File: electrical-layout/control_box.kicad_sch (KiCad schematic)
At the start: 5 parts, among them U14 PCB03, U18 NO Switch

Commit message: layout-2025: update many parts of the layout
What a goooood commit message!

... sorry
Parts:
- removed F6: 15A, symbol Device:Fuse
- removed U18: NO Switch, symbol Exocet:VC_Switch_NO
- added J6: Telemetry Battery Charge Connector, symbol Connector_Generic:Conn_01x02
- added J7: Tracking Device Connector, symbol Connector_Generic:Conn_01x02
- added K6: Telemetry Battery Relay, symbol Relay:Relay_SPST-NO
- added U12, U13, U9: Valve Actuator, symbol Exocet:Hanbay_Valve_Actuator
- added U24: Connection PCB, symbol Exocet:Connection_PCB
- added U25, U26: Temperature Sensor, Package_TO_SOT_THT:TO-92_Inline, symbol Sensor_Temperature:DS18B20
- added U27: H2 Control PCB, symbol Exocet:H2_Control_Pcb
- added U28, U29: Manometer, symbol Exocet:Swagelok_Manometer
- added U4: (no value), symbol Exocet:Power_Control_Pcb
- U14: value PCB03 -> Telemetry Battery PCB; DIST (none) -> JLCPCB; MFR (none) -> Exocet; MPN (none) -> PCB03
- U15: value ~ -> Cooling System; Manufacturer TBD -> (none); Part TBD -> (none)
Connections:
- net +48V: now also U4. (GATE); no longer U15. (GND)
- net GND: now also U4. (GATE); no longer U15. (GND)
- net at BT3.1 (+): now also J6.2 (Pin_2), K6.14
- net Frame: now reaches BT3.2 (-), U14. (GND)
- net Frame: now also J6.1 (Pin_1), J7.2 (Pin_2), K6.A2
- new net: U14. (GND), U25.1 (GND)
- new net: U14. (GND), U25.2 (DQ)
- new net: U14. (GND), U25.3 (V_{DD})
- new net: J7.1 (Pin_1), K6.13, U14. (GND)
- new net: U15. (GND), U26.1 (GND)
- new net: U15. (GND), U26.2 (DQ)
- new net: U15. (GND), U26.3 (V_{DD})
- new net BOP+: U15. (GND)
- new net BOP_CTRL_G: U4. (GATE)
- new net BOP_CTRL_S: U4. (GATE)
- new net BRAKE_CTRL_G: U4. (GATE)
- new net BRAKE_CTRL_S: U4. (GATE)
- new net CHARGE_UART: U4. (GATE)
- new net FC_CTRL_G: U4. (GATE)
- new net FC_CTRL_S: U4. (GATE)
- new net FC_UART: U4. (GATE)
- new net HV_BUS-: U15. (GND)
- new net MOTOR_CTRL_G: U4. (GATE)
- new net MOTOR_CTRL_S: U4. (GATE)
- no-connect marks 0 -> 24

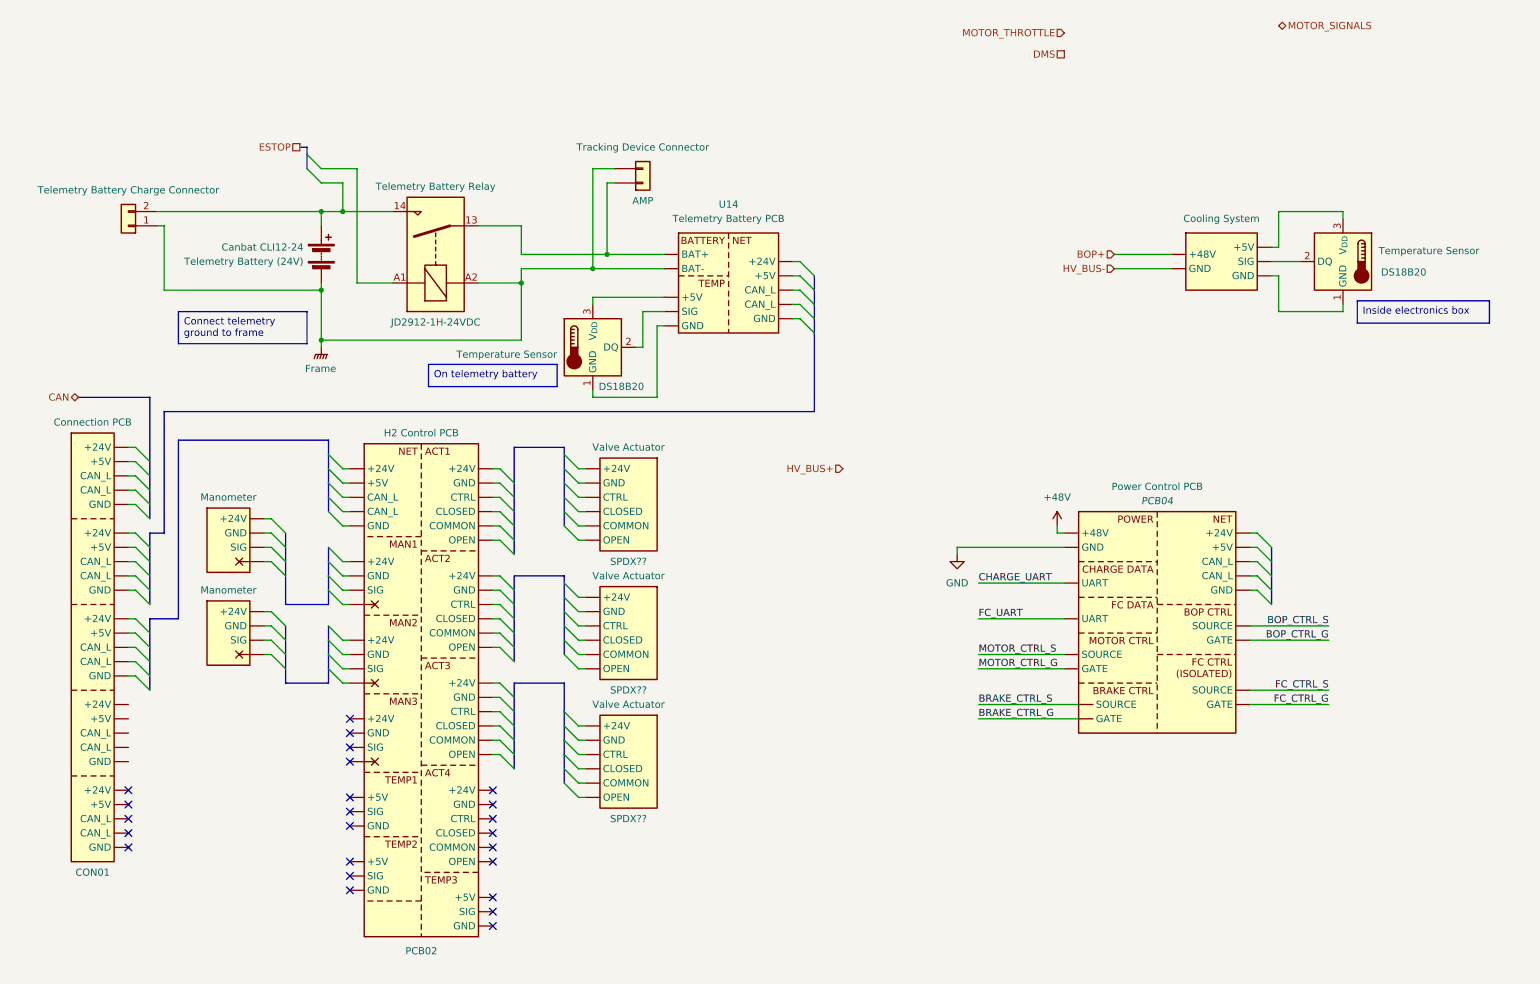
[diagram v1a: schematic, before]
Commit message: layout-2025: add power breadboard and connections
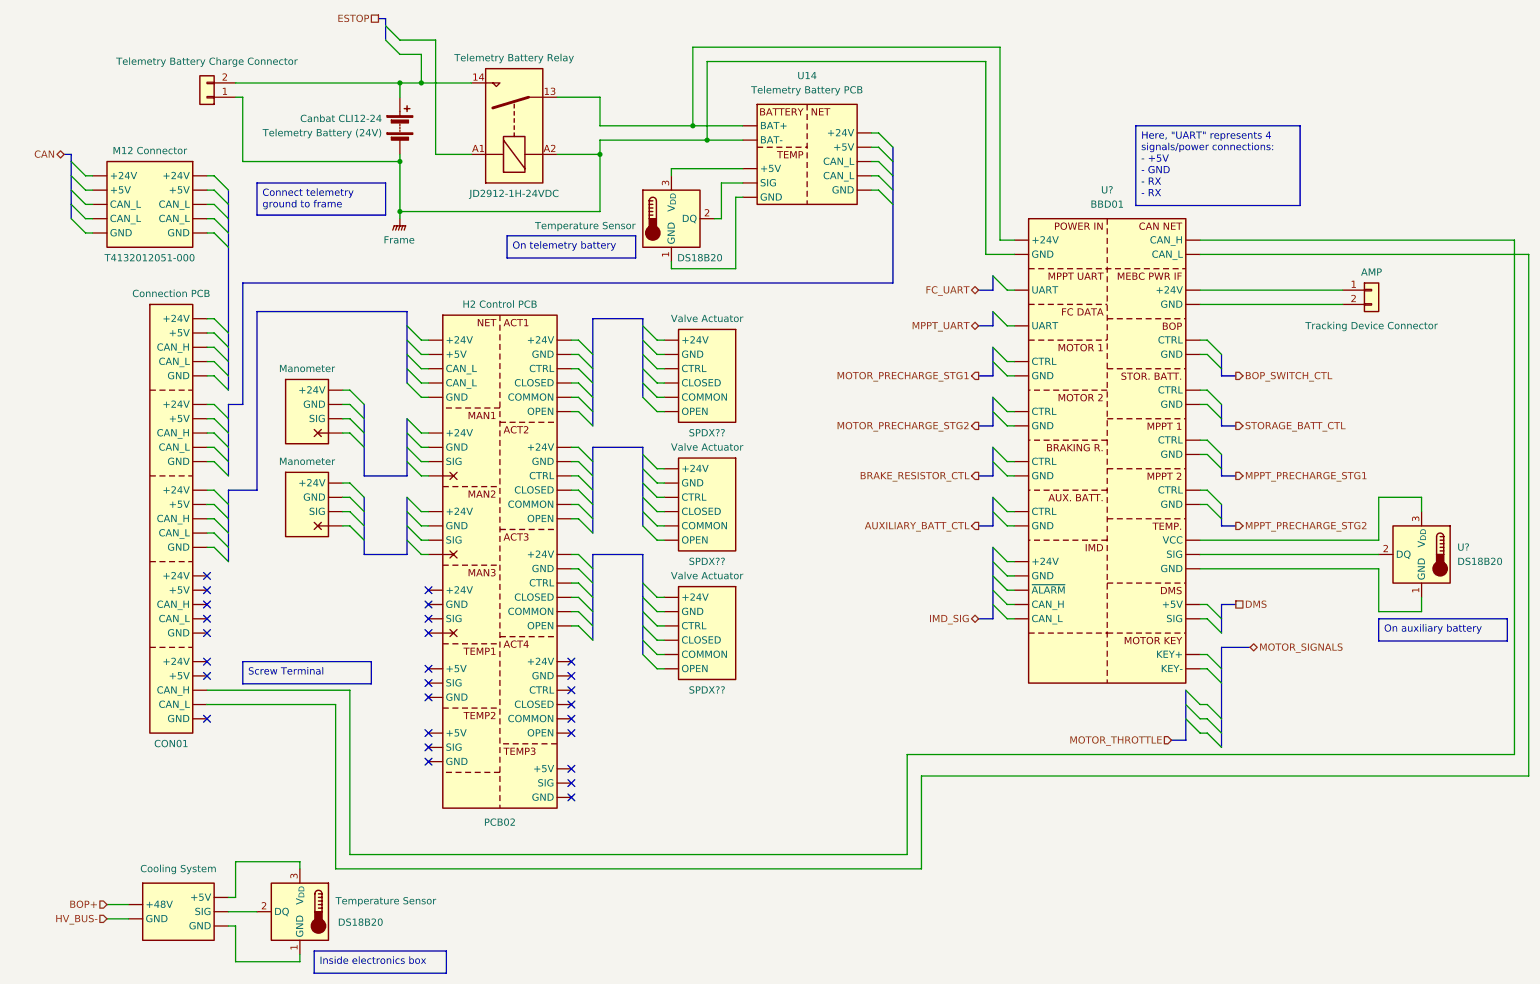
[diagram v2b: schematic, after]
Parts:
- removed U4: (no value), symbol Exocet:Power_Control_Pcb
- added J?: M12 Connector, symbol Exocet:M12_Connector
- added U?: DS18B20, Package_TO_SOT_THT:TO-92_Inline, symbol Sensor_Temperature:DS18B20
- added U?: BBD01, symbol Exocet:Power_Control_Breadboard
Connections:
- net Frame: now also U?. (KEY-); no longer J7.2 (Pin_2)
- net at U24. (GND): now also U?. (KEY-)
- new net: U?. (KEY-), U?.1 (GND)
- new net: U?. (KEY-), U?.2 (DQ)
- new net: U?. (KEY-), U?.3 (V_{DD})
- new net: K6.13, U14. (GND), U?. (KEY-)
- new net: J7.1 (Pin_1), U?. (KEY-)
- new net: J7.2 (Pin_2), U?. (KEY-)
- new net: U24. (GND), U?. (KEY-)
- no-connect marks 24 -> 27
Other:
- moved on the sheet: U14
